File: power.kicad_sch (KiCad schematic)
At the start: 0 parts

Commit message: add: moved power mgmt from old schematic
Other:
- added sheet Management (power_mgmt.kicad_sch)
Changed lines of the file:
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@@
 		(comment 1 "Elie Baier")
 	)
+	(sheet
+		(at 305.435 81.915)
+		(size 66.675 13.97)
+		(exclude_from_sim no)
+		(in_bom yes)
+		(on_board yes)
+		(dnp no)
+		(fields_autoplaced yes)
+		(stroke
+			(width 0.1524)
+			(type solid)
+		)
+		(fill
+			(color 0 0 0 0.0000)
+		)
+		(property "Sheetname" "Management"
+			(at 305.435 81.2034 0)
+			(effects
+				(font
+					(size 1.27 1.27)
+				)
+				(justify left bottom)
+			)
+		)
+		(property "Sheetfile" "power_mgmt.kicad_sch"
+			(at 305.435 96.4696 0)
+			(effects
+				(font
+					(size 1.27 1.27)
+				)
+				(justify left top)
+			)
+		)
+		(instances
+			(project "spine"
+				(path "/9b29516b-1745-41d0-bc5f-f6cf48cfb4af/19f231c9-3ea2-4c72-8861-e175feaab368"
+					(page "4")
+				)
+			)
+		)
+	)
 )

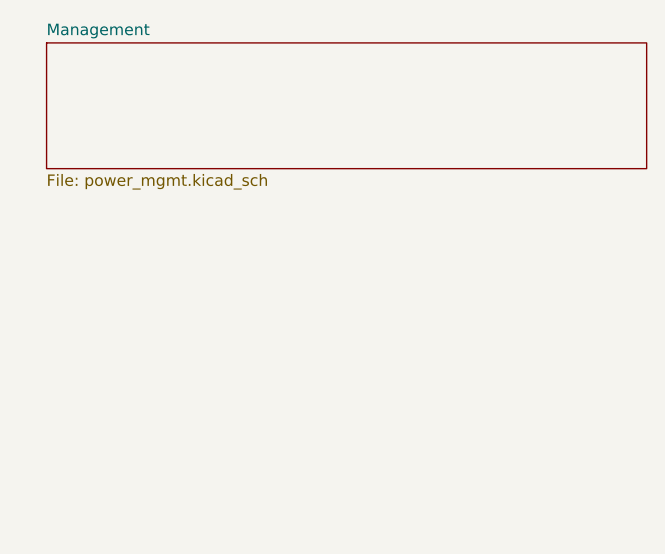
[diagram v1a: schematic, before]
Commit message: add: power MUX + global labels
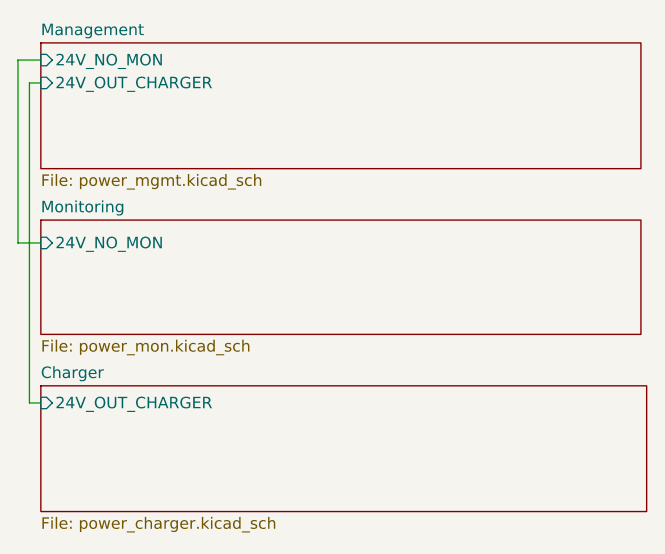
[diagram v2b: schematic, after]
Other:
- added sheet Charger (power_charger.kicad_sch)
- added sheet Monitoring (power_mon.kicad_sch)
- sheet Management ports: added 24V_NO_MON, 24V_OUT_CHARGER; removed none
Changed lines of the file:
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@@
 		(comment 1 "Elie Baier")
 	)
+	(wire
+		(pts
+			(xy 303.53 86.36) (xy 303.53 121.92)
+		)
+		(stroke
+			(width 0)
+			(type default)
+		)
+	)
+	(wire
+		(pts
+			(xy 304.8 86.36) (xy 303.53 86.36)
+		)
+		(stroke
+			(width 0)
+			(type default)
+		)
+	)
+	(wire
+		(pts
+			(xy 302.26 83.82) (xy 302.26 104.14)
+		)
+		(stroke
+			(width 0)
+			(type default)
+		)
+	)
+	(wire
+		(pts
+			(xy 302.26 104.14) (xy 304.8 104.14)
+		)
+		(stroke
+			(width 0)
+			(type default)
+		)
+	)
+	(wire
+		(pts
+			(xy 303.53 121.92) (xy 304.8 121.92)
+		)
+		(stroke
+			(width 0)
+			(type default)
+		)
+	)
+	(wire
+		(pts
+			(xy 304.8 83.82) (xy 302.26 83.82)
+		)
+		(stroke
+			(width 0)
+			(type default)
+		)
+	)
 	(sheet
-		(at 305.435 81.915)
+		(at 304.8 101.6)
+		(size 66.675 12.7)
+		(exclude_from_sim no)
+		(in_bom yes)
+		(on_board yes)
+		(dnp no)
+		(fields_autoplaced yes)
+		(stroke
+			(width 0.1524)
+			(type solid)
+		)
+		(fill
+			(color 0 0 0 0.0000)
+		)
+		(property "Sheetname" "Monitoring"
+			(at 304.8 100.8884 0)
+			(effects
+				(font
+					(size 1.27 1.27)
+				)
+				(justify left bottom)
+			)
+		)
+		(property "Sheetfile" "power_mon.kicad_sch"
+			(at 304.8 114.8846 0)
+			(effects
+				(font
+					(size 1.27 1.27)
+				)
+				(justify left top)
+			)
+		)
+		(pin "24V_NO_MON" input
+			(at 304.8 104.14 180)
+			(effects
+				(font
+					(size 1.27 1.27)
+				)
+				(justify left)
+			)
+		)
+		(instances
+			(project "spine"
+				(path "/9b29516b-1745-41d0-bc5f-f6cf48cfb4af/19f231c9-3ea2-4c72-8861-e175feaab368"
+					(page "5")
+				)
+			)
+		)
+	)
+	(sheet
+		(at 304.8 81.915)
 		(size 66.675 13.97)
 		(exclude_from_sim no)
@@
 		)
 		(property "Sheetname" "Management"
-			(at 305.435 81.2034 0)
+			(at 304.8 81.2034 0)
 			(effects
 				(font
@@
 		)
 		(property "Sheetfile" "power_mgmt.kicad_sch"
-			(at 305.435 96.4696 0)
+			(at 304.8 96.4696 0)
 			(effects
 				(font
@@
 				)
 				(justify left top)
+			)
+		)
+		(pin "24V_NO_MON" input
+			(at 304.8 83.82 180)
+			(effects
+				(font
+					(size 1.27 1.27)
+				)
+				(justify left)
+			)
+		)
+		(pin "24V_OUT_CHARGER" input
+			(at 304.8 86.36 180)
+			(effects
+				(font
+					(size 1.27 1.27)
+				)
+				(justify left)
 			)
 		)
@@
 				)
 			)
+		)
+	)
+	(sheet
+		(at 304.8 120.015)
+		(size 67.31 13.97)
+		(exclude_from_sim no)
+		(in_bom yes)
+		(on_board yes)
+		(dnp no)
+		(fields_autoplaced yes)
+		(stroke
+			(width 0.1524)
+			(type solid)
+		)
+		(fill
+			(color 0 0 0 0.0000)
+		)
+		(property "Sheetname" "Charger"
+			(at 304.8 119.3034 0)
+			(effects
+				(font
+					(size 1.27 1.27)
+				)
+				(justify left bottom)
+			)
+		)
+		(property "Sheetfile" "power_charger.kicad_sch"
+			(at 304.8 134.5696 0)
+			(effects
+				(font
+					(size 1.27 1.27)
+				)
+				(justify left top)
+			)
+		)
+		(pin "24V_OUT_CHARGER" input
+			(at 304.8 121.92 180)
+			(effects
+				(font
+					(size 1.27 1.27)
+				)
+				(justify left)
+			)
+		)
+		(instances
+			(project "spine"
+				(path "/9b29516b-1745-41d0-bc5f-f6cf48cfb4af/19f231c9-3ea2-4c72-8861-e175feaab368"
+					(page "6")
+				)
+			)
